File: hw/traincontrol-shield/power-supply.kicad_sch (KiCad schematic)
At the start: 9 parts, among them U1 MP2359DJ

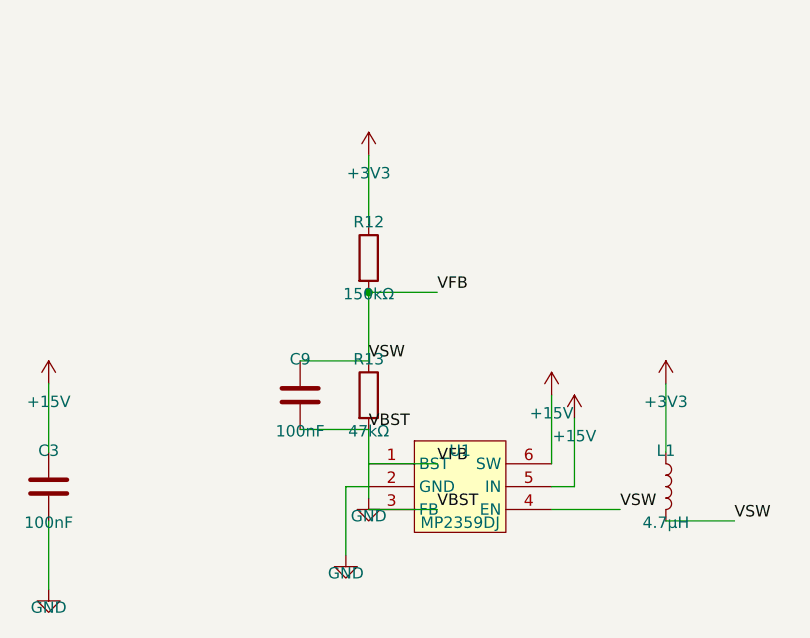
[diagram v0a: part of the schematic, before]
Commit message: Apply omnidirectional spacing rule: move R12/R13 divider above U1
R13 body bottom was only 2.54mm above U1 body top — violates the
IC-to-passive body-edge gap minimum of 2×STUB = 15.24mm.

Move R12/R13 up so R13 body bottom sits exactly 15.24mm above U1:
  R13 centre y: 58.42 → 45.72  (body bottom 48.26 → gap 15.24mm ✓)
  R12 centre y: 43.18 → 30.48  (maintains 15.24mm centre spacing to R13)

All other sheets audited — no other vertical violations found.
All 8 schematics regenerated and validated (kicad-cli PASS).

Co-Authored-By: Claude Sonnet 4.6 <noreply@anthropic.com>
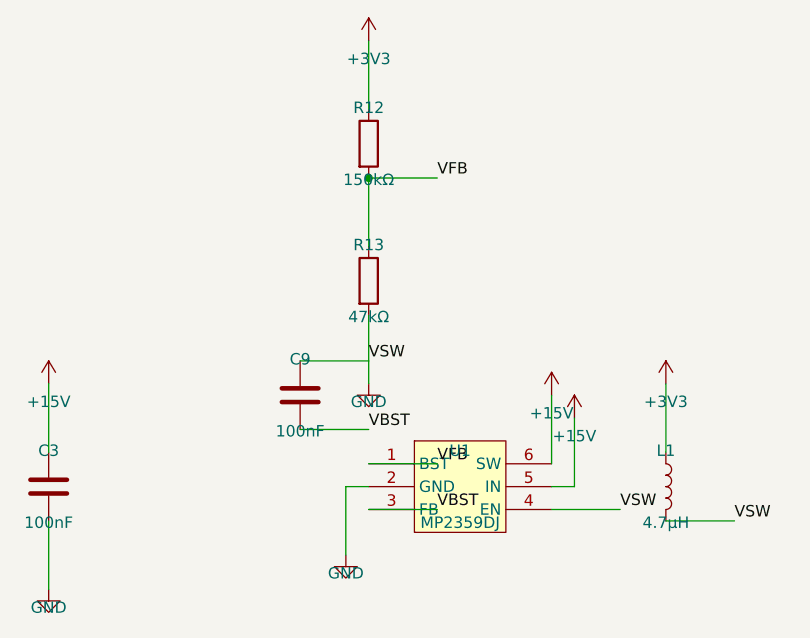
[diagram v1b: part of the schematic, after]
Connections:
- net GND: now also C9.1, L1.2, U1.4 (EN); no longer C9.2, U1.3 (FB)
- net VFB: no longer C9.1, L1.2, U1.4 (EN)
- new net VBST: C9.2, U1.3 (FB)
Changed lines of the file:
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@@
 	(symbol
 		(lib_id "Device:R")
-		(at 157.48 43.18 0)
+		(at 157.48 30.48 0)
 		(unit 1)
 		(exclude_from_sim no)
@@
 		(dnp no)
 		(property "Reference" "R12"
-			(at 157.48 39.18 0)
+			(at 157.48 26.48 0)
 			(effects (font (size 1.27 1.27)))
 		)
 		(property "Value" "150kΩ"
-			(at 157.48 47.18 0)
+			(at 157.48 34.480000000000004 0)
 			(effects (font (size 1.27 1.27)))
 		)
 		(property "Footprint" "Resistor_SMD:R_0603_1608Metric"
-			(at 157.48 43.18 0)
+			(at 157.48 30.48 0)
 			(effects (font (size 1.27 1.27)) (hide yes))
 		)
 		(property "Datasheet" "~"
-			(at 157.48 43.18 0)
+			(at 157.48 30.48 0)
 			(effects (font (size 1.27 1.27)) (hide yes))
 		)
@@
 	(symbol
 		(lib_id "Device:R")
-		(at 157.48 58.42 0)
+		(at 157.48 45.72 0)
 		(unit 1)
 		(exclude_from_sim no)
@@
 		(dnp no)
 		(property "Reference" "R13"
-			(at 157.48 54.42 0)
+			(at 157.48 41.72 0)
 			(effects (font (size 1.27 1.27)))
 		)
 		(property "Value" "47kΩ"
-			(at 157.48 62.42 0)
+			(at 157.48 49.72 0)
 			(effects (font (size 1.27 1.27)))
 		)
 		(property "Footprint" "Resistor_SMD:R_0603_1608Metric"
-			(at 157.48 58.42 0)
+			(at 157.48 45.72 0)
 			(effects (font (size 1.27 1.27)) (hide yes))
 		)
 		(property "Datasheet" "~"
-			(at 157.48 58.42 0)
+			(at 157.48 45.72 0)
 			(effects (font (size 1.27 1.27)) (hide yes))
 		)
@@
 	)
 	(wire
-		(pts (xy 157.48 39.37) (xy 157.48 31.749999999999996))
+		(pts (xy 157.48 26.67) (xy 157.48 19.05))
 		(stroke (width 0) (type solid))
 	)
 	(symbol
 		(lib_id "power:+3V3")
-		(at 157.48 31.749999999999996 0)
+		(at 157.48 19.05 0)
 		(unit 1)
 		(exclude_from_sim no)
@@
 		(dnp no)
 		(property "Reference" "#PWR0213"
-			(at 157.48 29.749999999999996 0)
+			(at 157.48 17.05 0)
 			(effects (font (size 1.27 1.27)) (hide yes))
 		)
 		(property "Value" "+3V3"
-			(at 157.48 33.75 0)
-			(effects (font (size 1.27 1.27)))
-		)
-		(property "Footprint" ""
-			(at 157.48 31.749999999999996 0)
-			(effects (font (size 1.27 1.27)) (hide yes))
-		)
-		(property "Datasheet" ""
-			(at 157.48 31.749999999999996 0)
+			(at 157.48 21.05 0)
+			(effects (font (size 1.27 1.27)))
+		)
+		(property "Footprint" ""
+			(at 157.48 19.05 0)
+			(effects (font (size 1.27 1.27)) (hide yes))
+		)
+		(property "Datasheet" ""
+			(at 157.48 19.05 0)
 			(effects (font (size 1.27 1.27)) (hide yes))
 		)
@@
 	)
 	(wire
-		(pts (xy 157.48 62.23) (xy 157.48 69.85))
+		(pts (xy 157.48 49.53) (xy 157.48 57.15))
 		(stroke (width 0) (type solid))
 	)
 	(symbol
 		(lib_id "power:GND")
-		(at 157.48 69.85 0)
+		(at 157.48 57.15 0)
 		(unit 1)
 		(exclude_from_sim no)
@@
 		(dnp no)
 		(property "Reference" "#PWR0214"
-			(at 157.48 67.85 0)
+			(at 157.48 55.15 0)
 			(effects (font (size 1.27 1.27)) (hide yes))
 		)
 		(property "Value" "GND"
-			(at 157.48 71.85 0)
-			(effects (font (size 1.27 1.27)))
-		)
-		(property "Footprint" ""
-			(at 157.48 69.85 0)
-			(effects (font (size 1.27 1.27)) (hide yes))
-		)
-		(property "Datasheet" ""
-			(at 157.48 69.85 0)
+			(at 157.48 59.15 0)
+			(effects (font (size 1.27 1.27)))
+		)
+		(property "Footprint" ""
+			(at 157.48 57.15 0)
+			(effects (font (size 1.27 1.27)) (hide yes))
+		)
+		(property "Datasheet" ""
+			(at 157.48 57.15 0)
 			(effects (font (size 1.27 1.27)) (hide yes))
 		)
@@
 	)
 	(wire
-		(pts (xy 157.48 46.99) (xy 157.48 54.61))
+		(pts (xy 157.48 34.29) (xy 157.48 41.91))
 		(stroke (width 0) (type solid))
 	)
@@
 	)
 	(wire
-		(pts (xy 157.48 46.99) (xy 165.1 46.99))
+		(pts (xy 157.48 34.29) (xy 165.1 34.29))
 		(stroke (width 0) (type solid))
 	)
 	(label "VFB"
-		(at 165.1 46.99 0)
+		(at 165.1 34.29 0)
 		(fields_autoplaced yes)
 		(effects (font (size 1.27 1.27)) (justify left bottom))
@@
 	)
 	(junction
-		(at 157.48 46.99)
+		(at 157.48 34.29)
 		(diameter 0)
 		(color 0 0 0 0)

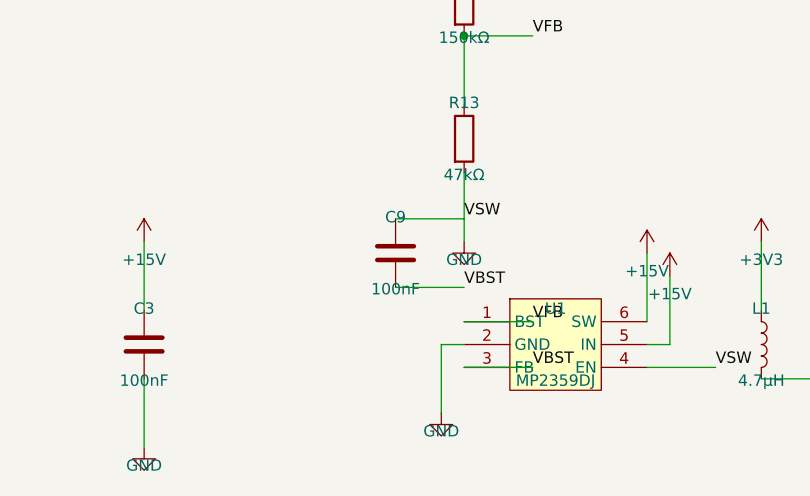
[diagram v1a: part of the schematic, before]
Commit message: Fix U1 left-side net_label direction; move C9 clear of pin column
Issue 1 — C9 was placed only 1×STUB left of U1's BST/GND/FB pin column
(x=149.86), causing its net_label stubs to land exactly at U1's pin tips
(x=157.48), visually grouping C9 with U1.  Move C9 left by 2×STUB:
  x: 149.86 → 134.62  (stubs now end at 142.24, 15.24mm clear of pins) ✓

Issue 2 — VBST and VFB net_labels on U1's left-side pins (BST pin1,
FB pin3) used angle=0, so their stubs pointed RIGHT into the IC body.
Changed to angle=180 so stubs point LEFT (away from IC), matching the
left-exit direction of those pins.

Co-Authored-By: Claude Sonnet 4.6 <noreply@anthropic.com>
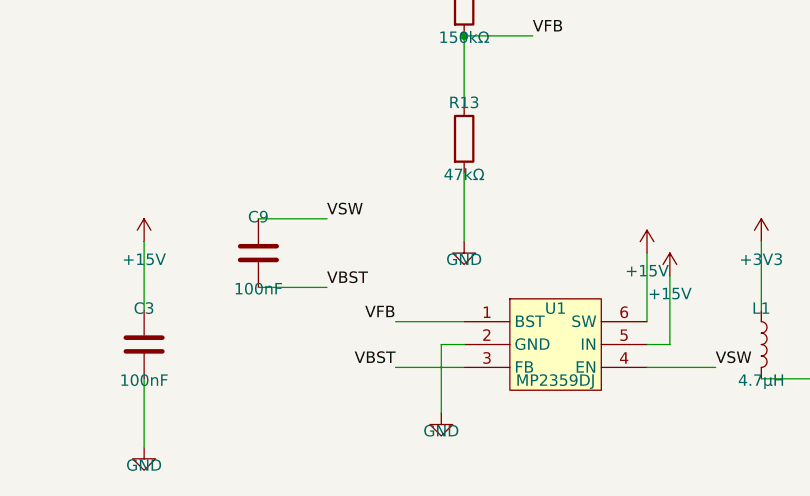
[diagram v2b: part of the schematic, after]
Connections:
- net GND: no longer C9.1, L1.2, U1.4 (EN)
- new net VSW: C9.1, L1.2, U1.4 (EN)
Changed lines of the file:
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@@
 	(symbol
 		(lib_id "Device:C")
-		(at 149.86 58.42 0)
+		(at 134.62 58.42 0)
 		(unit 1)
 		(exclude_from_sim no)
@@
 		(dnp no)
 		(property "Reference" "C9"
-			(at 149.86 54.42 0)
+			(at 134.62 54.42 0)
 			(effects (font (size 1.27 1.27)))
 		)
 		(property "Value" "100nF"
-			(at 149.86 62.42 0)
+			(at 134.62 62.42 0)
 			(effects (font (size 1.27 1.27)))
 		)
 		(property "Footprint" "Capacitor_SMD:C_0603_1608Metric"
-			(at 149.86 58.42 0)
+			(at 134.62 58.42 0)
 			(effects (font (size 1.27 1.27)) (hide yes))
 		)
 		(property "Datasheet" "~"
-			(at 149.86 58.42 0)
+			(at 134.62 58.42 0)
 			(effects (font (size 1.27 1.27)) (hide yes))
 		)
@@
 	)
 	(wire
-		(pts (xy 157.48 71.12) (xy 165.1 71.12))
+		(pts (xy 149.85999999999999 71.12) (xy 157.48 71.12))
 		(stroke (width 0) (type solid))
 	)
 	(label "VBST"
-		(at 165.1 71.12 0)
+		(at 149.85999999999999 71.12 180)
 		(fields_autoplaced yes)
-		(effects (font (size 1.27 1.27)) (justify left bottom))
-	)
-	(wire
-		(pts (xy 149.86 62.23) (xy 157.48000000000002 62.23))
+		(effects (font (size 1.27 1.27)) (justify right bottom))
+	)
+	(wire
+		(pts (xy 134.62 62.23) (xy 142.24 62.23))
 		(stroke (width 0) (type solid))
 	)
 	(label "VBST"
-		(at 157.48000000000002 62.23 0)
+		(at 142.24 62.23 0)
 		(fields_autoplaced yes)
 		(effects (font (size 1.27 1.27)) (justify left bottom))
@@
 	)
 	(wire
-		(pts (xy 149.86 54.61) (xy 157.48000000000002 54.61))
+		(pts (xy 134.62 54.61) (xy 142.24 54.61))
 		(stroke (width 0) (type solid))
 	)
 	(label "VSW"
-		(at 157.48000000000002 54.61 0)
+		(at 142.24 54.61 0)
 		(fields_autoplaced yes)
 		(effects (font (size 1.27 1.27)) (justify left bottom))
@@
 	)
 	(wire
-		(pts (xy 157.48 66.04) (xy 165.1 66.04))
+		(pts (xy 149.85999999999999 66.04) (xy 157.48 66.04))
 		(stroke (width 0) (type solid))
 	)
 	(label "VFB"
-		(at 165.1 66.04 0)
+		(at 149.85999999999999 66.04 180)
 		(fields_autoplaced yes)
-		(effects (font (size 1.27 1.27)) (justify left bottom))
-	)
-	(wire
+		(effects (font (size 1.27 1.27)) (justify right bottom))
+	)
+	(wire

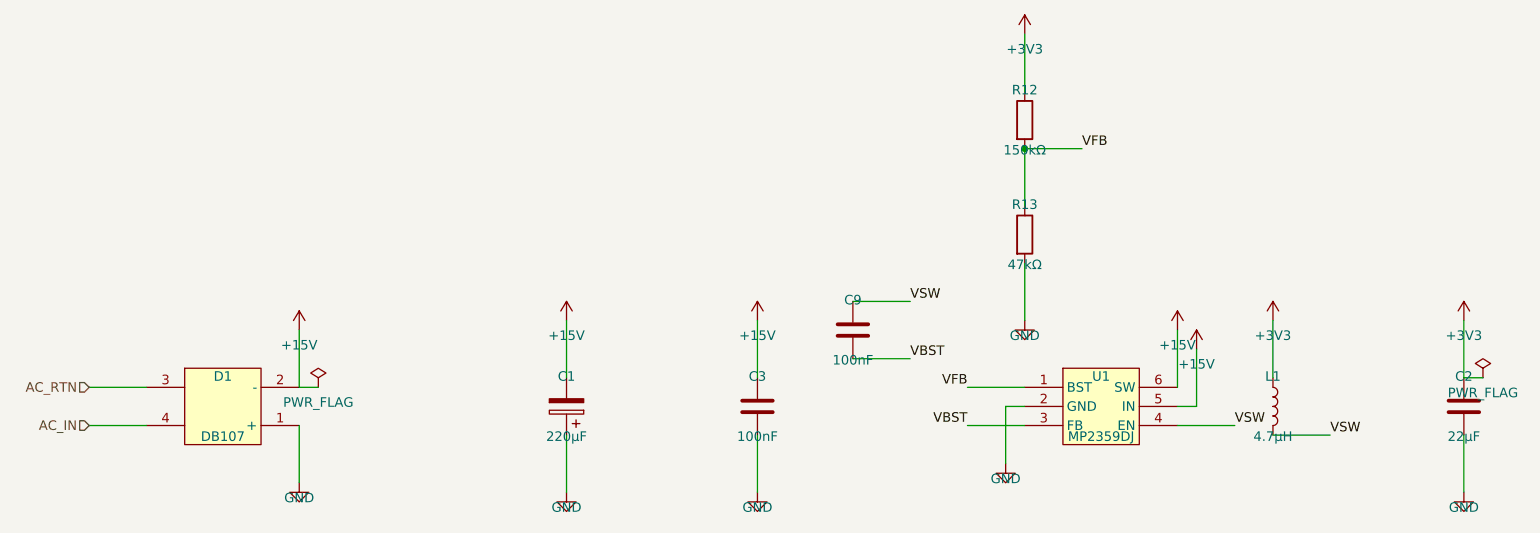
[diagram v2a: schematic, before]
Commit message: Fix schematic ERC errors: pin Y-flip, PWR_FLAG, label wiring, spacing
- Fix connector pin positions using Y-flip convention (sym Y-up → sch Y-down)
- Add GND PWR_FLAG to power-supply sheet (eliminates power_pin_not_driven)
- Fix top-level connector label placement: labels at stub end, wires toward pins
- Apply omnidirectional spacing and IC-to-passive body gap rules across sheets
- Update schematics-plan.md with ERC workflow and coordinate conventions
- Regenerate all sub-sheets with corrected generator scripts

ERC result: 138 violations (all warnings/cosmetic), 0 critical errors.

Co-Authored-By: Claude Opus 4.6 <noreply@anthropic.com>
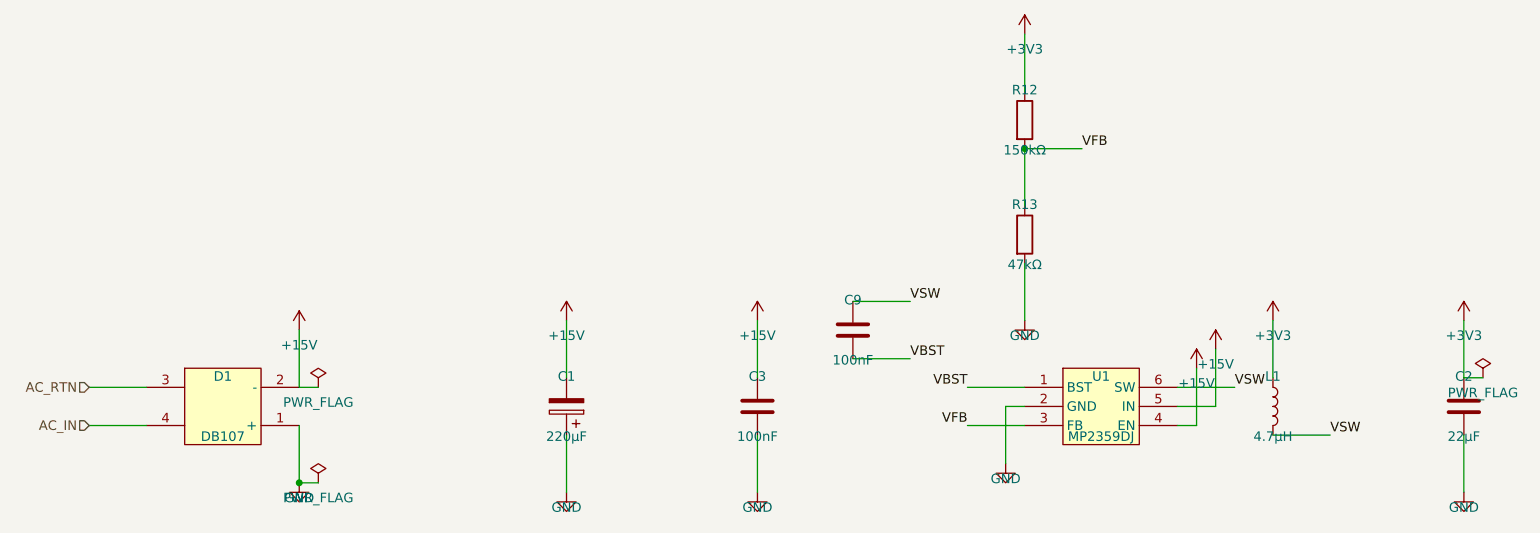
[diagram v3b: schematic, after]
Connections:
- net +15V: now also U1.4 (EN); no longer U1.6 (SW)
- net VBST: now also U1.1 (BST); no longer U1.3 (FB)
- net VFB: now also U1.3 (FB); no longer U1.1 (BST)
- net VSW: now also U1.6 (SW); no longer U1.4 (EN)
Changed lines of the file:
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@@
 	)
 	(wire
-		(pts (xy 177.8 66.04) (xy 177.8 58.42000000000001))
+		(pts (xy 177.8 71.12) (xy 180.34 71.12))
+		(stroke (width 0) (type solid))
+	)
+	(wire
+		(pts (xy 180.34 71.12) (xy 180.34 63.50000000000001))
 		(stroke (width 0) (type solid))
 	)
 	(symbol
 		(lib_id "power:+15V")
-		(at 177.8 58.42000000000001 0)
+		(at 180.34 63.50000000000001 0)
 		(unit 1)
 		(exclude_from_sim no)
@@
 		(dnp no)
 		(property "Reference" "#PWR0208"
-			(at 177.8 56.42000000000001 0)
+			(at 180.34 61.50000000000001 0)
 			(effects (font (size 1.27 1.27)) (hide yes))
 		)
 		(property "Value" "+15V"
-			(at 177.8 60.42000000000001 0)
-			(effects (font (size 1.27 1.27)))
-		)
-		(property "Footprint" ""
-			(at 177.8 58.42000000000001 0)
-			(effects (font (size 1.27 1.27)) (hide yes))
-		)
-		(property "Datasheet" ""
-			(at 177.8 58.42000000000001 0)
+			(at 180.34 65.5 0)
+			(effects (font (size 1.27 1.27)))
+		)
+		(property "Footprint" ""
+			(at 180.34 63.50000000000001 0)
+			(effects (font (size 1.27 1.27)) (hide yes))
+		)
+		(property "Datasheet" ""
+			(at 180.34 63.50000000000001 0)
 			(effects (font (size 1.27 1.27)) (hide yes))
 		)
@@
 	)
 	(wire
-		(pts (xy 177.8 68.58) (xy 180.34 68.58))
-		(stroke (width 0) (type solid))
-	)
-	(wire
-		(pts (xy 180.34 68.58) (xy 180.34 60.96))
+		(pts (xy 177.8 68.58) (xy 182.88 68.58))
+		(stroke (width 0) (type solid))
+	)
+	(wire
+		(pts (xy 182.88 68.58) (xy 182.88 60.96))
 		(stroke (width 0) (type solid))
 	)
 	(symbol
 		(lib_id "power:+15V")
-		(at 180.34 60.96 0)
+		(at 182.88 60.96 0)
 		(unit 1)
 		(exclude_from_sim no)
@@
 		(dnp no)
 		(property "Reference" "#PWR0209"
-			(at 180.34 58.96 0)
+			(at 182.88 58.96 0)
 			(effects (font (size 1.27 1.27)) (hide yes))
 		)
 		(property "Value" "+15V"
-			(at 180.34 62.96 0)
-			(effects (font (size 1.27 1.27)))
-		)
-		(property "Footprint" ""
-			(at 180.34 60.96 0)
-			(effects (font (size 1.27 1.27)) (hide yes))
-		)
-		(property "Datasheet" ""
-			(at 180.34 60.96 0)
+			(at 182.88 62.96 0)
+			(effects (font (size 1.27 1.27)))
+		)
+		(property "Footprint" ""
+			(at 182.88 60.96 0)
+			(effects (font (size 1.27 1.27)) (hide yes))
+		)
+		(property "Datasheet" ""
+			(at 182.88 60.96 0)
 			(effects (font (size 1.27 1.27)) (hide yes))
 		)
@@
 		)
 	)
+	(symbol
+		(lib_id "power:PWR_FLAG")
+		(at 63.5 78.74 0)
+		(unit 1)
+		(exclude_from_sim no)
+		(in_bom no)
+		(on_board yes)
+		(dnp no)
+		(property "Reference" "#PWR0217"
+			(at 63.5 76.74 0)
+			(effects (font (size 1.27 1.27)) (hide yes))
+		)
+		(property "Value" "PWR_FLAG"
+			(at 63.5 80.74 0)
+			(effects (font (size 1.27 1.27)))
+		)
+		(property "Footprint" ""
+			(at 63.5 78.74 0)
+			(effects (font (size 1.27 1.27)) (hide yes))
+		)
+		(property "Datasheet" ""
+			(at 63.5 78.74 0)
+			(effects (font (size 1.27 1.27)) (hide yes))
+		)
+		(pin "1")
+		(instances
+			(project "traincontrol-shield"
+				(path "/12cc2a67-9b1c-41e4-828f-9c2a8df6bb35/a7305cff-bbaf-4846-983d-83b0ea81fbce"
+					(reference "#PWR0217")
+					(unit 1)
+				)
+			)
+		)
+	)
 	(wire
 		(pts (xy 60.96 66.04) (xy 63.5 66.04))
@@
 	)
 	(wire
-		(pts (xy 149.85999999999999 71.12) (xy 157.48 71.12))
+		(pts (xy 60.96 78.74) (xy 63.5 78.74))
+		(stroke (width 0) (type solid))
+	)
+	(junction
+		(at 60.96 78.74)
+		(diameter 0)
+		(color 0 0 0 0)
+	)
+	(wire
+		(pts (xy 149.85999999999999 66.04) (xy 157.48 66.04))
 		(stroke (width 0) (type solid))
 	)
 	(label "VBST"
-		(at 149.85999999999999 71.12 180)
+		(at 149.85999999999999 66.04 180)
 		(fields_autoplaced yes)
 		(effects (font (size 1.27 1.27)) (justify right bottom))
@@
 	)
 	(wire
-		(pts (xy 177.8 71.12) (xy 185.42000000000002 71.12))
+		(pts (xy 177.8 66.04) (xy 185.42000000000002 66.04))
 		(stroke (width 0) (type solid))
 	)
 	(label "VSW"
-		(at 185.42000000000002 71.12 0)
+		(at 185.42000000000002 66.04 0)
 		(fields_autoplaced yes)
 		(effects (font (size 1.27 1.27)) (justify left bottom))
@@
 	)
 	(wire
-		(pts (xy 149.85999999999999 66.04) (xy 157.48 66.04))
+		(pts (xy 149.85999999999999 71.12) (xy 157.48 71.12))
 		(stroke (width 0) (type solid))
 	)
 	(label "VFB"
-		(at 149.85999999999999 66.04 180)
+		(at 149.85999999999999 71.12 180)
 		(fields_autoplaced yes)
 		(effects (font (size 1.27 1.27)) (justify right bottom))
